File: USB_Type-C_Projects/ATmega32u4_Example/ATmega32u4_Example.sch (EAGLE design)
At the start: 8 parts, among them J2 105450-0101, U1 ATMEGA32U4-AU, U2 IP4234CZ6,125

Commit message: USB connections made.
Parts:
- added C1: 1uF, MF_Passives:CAPACITOR_NP_0603
- added C10, C11, C12, C2, C7, C8, C9: 0.1uF, MF_Passives:CAPACITOR_NP_0603
- added C5, C6: 22pF, MF_Passives:CAPACITOR_NP_0603
- added R1: 5.1K, MF_Passives:RESISTOR_0603
- added R3: 22, MF_Passives:RESISTOR_0603
- added R4: 10K, MF_Passives:RESISTOR_0603
- added SW1: MF-SW-TACT-4.2MM, MF_Switches:TACT_4.2MM
- added X1: ABM3B-16.000MHZ-D-1-X-T, MF_Frequency_Control:CYRSTAL_GND_ABM3B
- C3: value 0.1uF -> 1uF; MPN MF-CAP-0603-0.1uF -> MF-CAP-0603-1uF
- C4: value 1uF -> 0.1uF; MPN MF-CAP-0603-1uF -> MF-CAP-0603-0.1uF
- R2: value 5.1K -> 22; MPN ERJ-3EKF5101V -> MF-RES-0603-22
- U1: value ATMEGA32U4-AU -> IP4234CZ6,125; device MF_IC_Digital:ATMEGA32U4-AU -> PP_Passives:IP4234CZ6; MPN (none) -> IP4234CZ6,125
- U2: value IP4234CZ6,125 -> ATMEGA32U4-AU; device PP_Passives:IP4234CZ6 -> MF_IC_Digital:ATMEGA32U4-AU; MPN IP4234CZ6,125 -> (none)
- renumbered L3 to L1, L4 to L2
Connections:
- new net N$1: R2.P$2, U2.D-
- new net N$2: R3.P$2, U2.D+
- new net N$3: C3.P$2, U2.UCAP
- new net N$4: C4.P$2, U2.AREF
- new net RESET: R4.P$2, SW1.P$1, SW1.P$2, U2.!RESET
- new net XTAL1: C5.P$1, U2.XTAL1, X1.X0
- new net XTAL2: C6.P$1, U2.XTAL2, X1.X1
- net CC1/1: now also R1.P$1; no longer R2.P$1
- net D+: now also U1.I/O1A; no longer U2.I/O1A
- net D-: now also U1.I/O1B; no longer U2.I/O1B
- net DM: now also R2.P$1, U1.I/O2B; no longer U2.I/O2B
- net DP: now also R3.P$1, U1.I/O2A; no longer U2.I/O2A
- net GND: now also C1.P$2, C10.P$2, C11.P$2, C12.P$2, C2.P$2, C3.P$1, C4.P$1, C5.P$2, C6.P$2, C7.P$2, C8.P$2, C9.P$2, R1.P$2, SW1.P$3, SW1.P$4, U1.GND, U2.UGND, X1.GND; no longer C3.P$2, C4.P$2, R2.P$2
- net USB_VBUS: now also C1.P$1, C10.P$1, C11.P$1, C12.P$1, C2.P$1, C7.P$1, C8.P$1, C9.P$1, R4.P$1, U1.VB, U2.AVCC, U2.UVCC, U2.VBUS, U2.VCC; no longer C3.P$1, C4.P$1, U2.VB
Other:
- moved on the sheet: C3, C4, R2

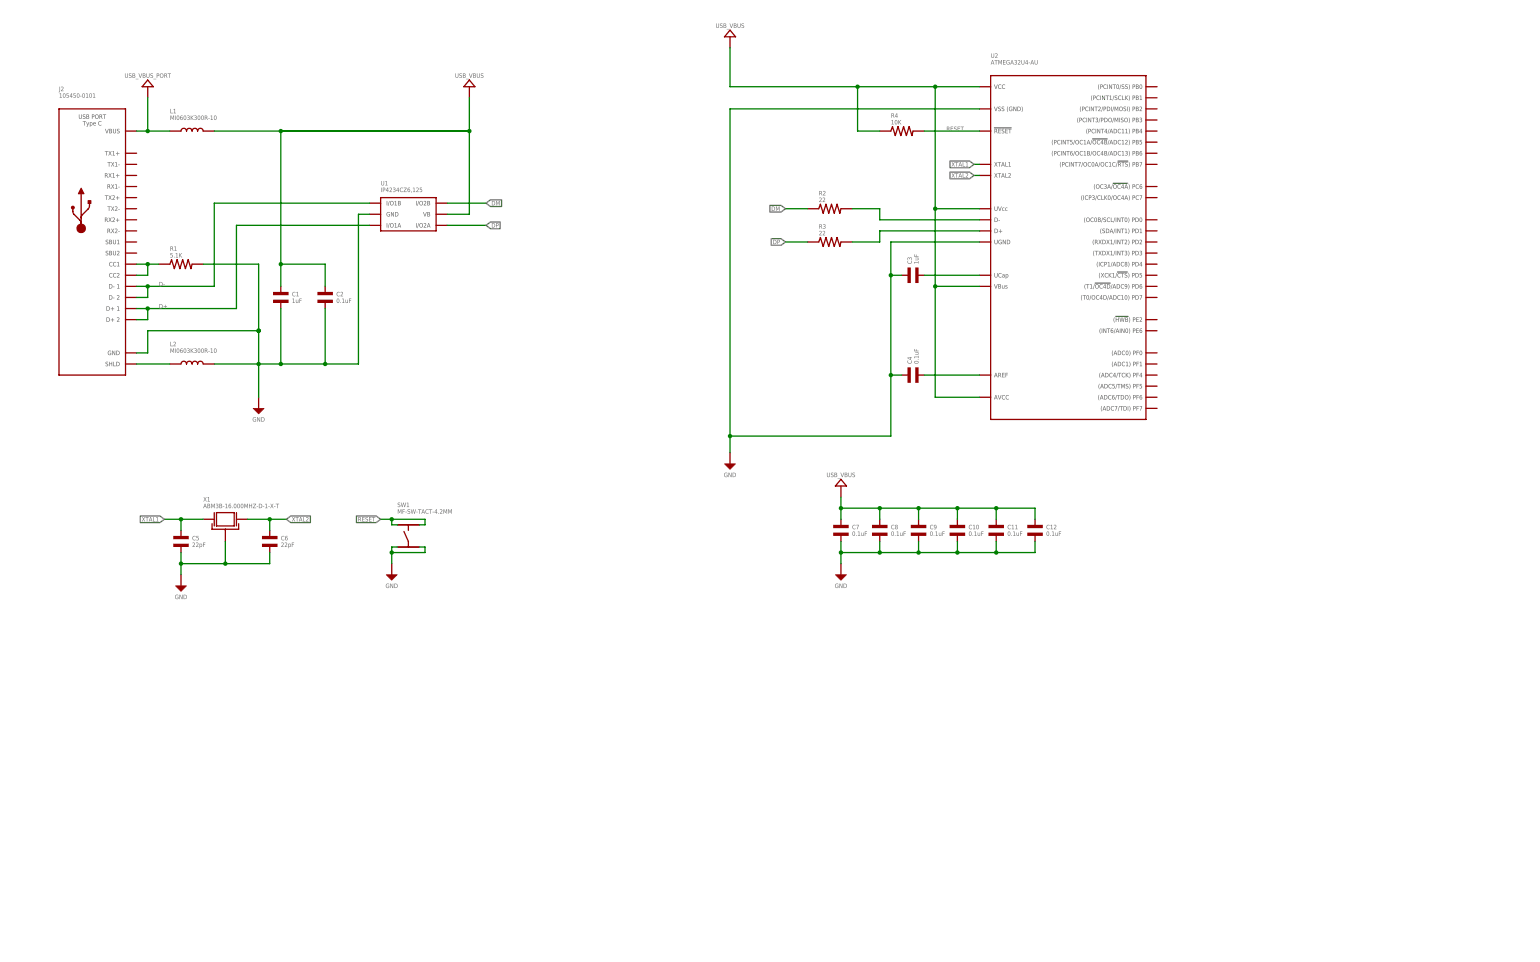
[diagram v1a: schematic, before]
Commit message: Schematic complete. Parts placed.
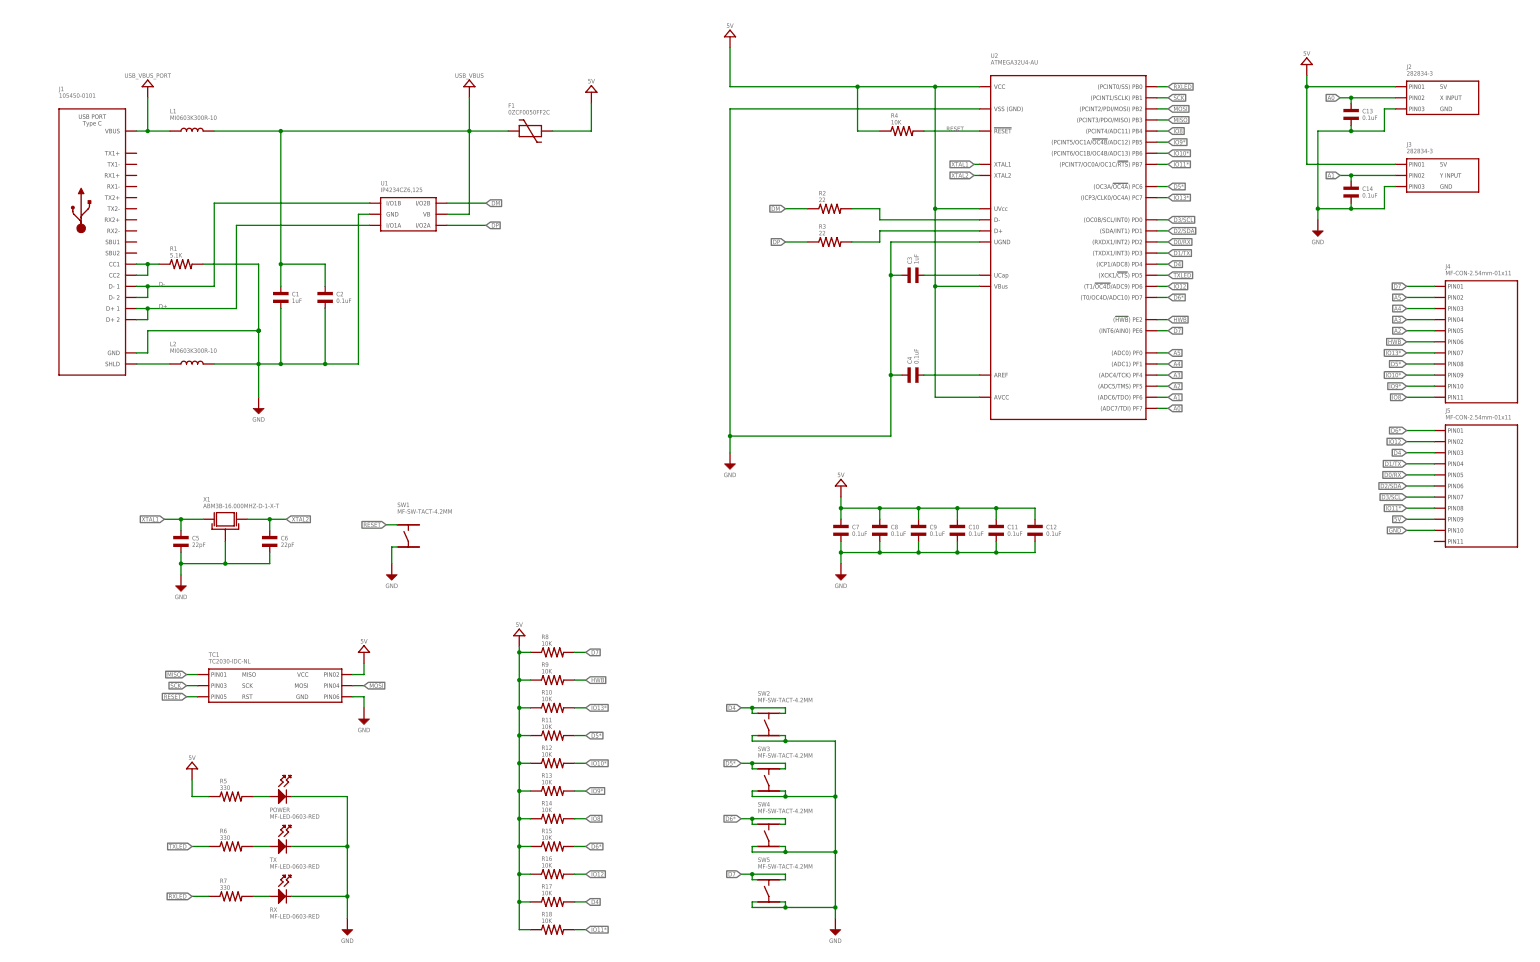
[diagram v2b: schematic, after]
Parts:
- added C13, C14: 0.1uF, MF_Passives:CAPACITOR_NP_0603
- added F1: 0ZCF0050FF2C, PP_Passives:PTC_FUSE_2920
- added J1: 105450-0101, PP_Connectors:USB_TYPE-C_105450-0101
- added J3: 282834-3, PP_Connectors:CON_01X03_282834-3
- added J4, J5: MF-CON-2.54mm-01x11, MF_Connectors:CON_01X11_PTH_2.54MM
- added POWER, RX, TX: MF-LED-0603-RED, MF_LEDs:LED_SINGLE-0603-RED
- added R10, R11, R12, R13, R14, R15, R16, R17, R18, R8, R9: 10K, MF_Passives:RESISTOR_0603
- added R5, R6, R7: 330, MF_Passives:RESISTOR_0603
- added SW2, SW3, SW4, SW5: MF-SW-TACT-4.2MM, MF_Switches:TACT_4.2MM
- added TC1: TC2030-IDC-NL, MF_Connectors:CON_02X03_AVRISP_TC2030-IDC-NL
- J2: value 105450-0101 -> 282834-3; device PP_Connectors:USB_TYPE-C_105450-0101 -> PP_Connectors:CON_01X03_282834-3; LABEL01 (none) -> 5V; LABEL02 (none) -> X INPUT; LABEL03 (none) -> GND; MPN 105450-0101 -> (none)
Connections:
- new net 5V: C10.P$1, C11.P$1, C12.P$1, C7.P$1, C8.P$1, C9.P$1, F1.P$2, J2.PIN1, J3.PIN1, J5.PIN9, R10.P$1, R11.P$1, R12.P$1, R13.P$1, R14.P$1, R15.P$1, R16.P$1, R17.P$1, R18.P$1, R4.P$1, R5.P$1, R8.P$1, R9.P$1, TC1.PIN2, U2.AVCC, U2.UVCC, U2.VBUS, U2.VCC
- new net A0: C13.P$1, J2.PIN2, U2.PF7
- new net A1: C14.P$1, J3.PIN2, U2.PF6
- new net A2: J4.PIN5, U2.PF5
- new net A3: J4.PIN4, U2.PF4
- new net A4: J4.PIN3, U2.PF1
- new net A5: J4.PIN2, U2.PF0
- new net D0/RX: J5.PIN5, U2.PD2
- new net D1/TX: J5.PIN4, U2.PD3
- new net D2/SDA: J5.PIN6, U2.PD1
- new net D3/SCL: J5.PIN7, U2.PD0
- new net D4: J5.PIN3, R17.P$2, SW2.P$1, SW2.P$2, U2.PD4
- new net D5*: J4.PIN8, R11.P$2, SW3.P$1, SW3.P$2, U2.PC6
- new net D6*: J5.PIN1, R15.P$2, SW4.P$1, SW4.P$2, U2.PD7
- new net D7: J4.PIN1, R8.P$2, SW5.P$1, SW5.P$2, U2.PE6
- new net HWB: J4.PIN6, R9.P$2, U2.PE2
- new net IO10*: J4.PIN9, R12.P$2, U2.PB6
- new net IO11*: J5.PIN8, R18.P$2, U2.PB7
- new net IO12: J5.PIN2, R16.P$2, U2.PD6
- new net IO13*: J4.PIN7, R10.P$2, U2.PC7
- new net IO8: J4.PIN11, R14.P$2, U2.PB4
- new net IO9*: J4.PIN10, R13.P$2, U2.PB5
- new net MISO: TC1.PIN1, U2.PB3
- new net MOSI: TC1.PIN4, U2.PB2
- new net N$5: POWER.ANODE, R5.P$2
- new net N$6: R6.P$2, TX.ANODE
- new net N$7: R7.P$2, RX.ANODE
- new net RXLED: R7.P$1, U2.PB0
- new net SCK: TC1.PIN3, U2.PB1
- new net TXLED: R6.P$1, U2.PD5
- net CC1/1: now also J1.CC1, J1.CC2; no longer J2.CC1, J2.CC2
- net D+: now also J1.D+1, J1.D+2; no longer J2.D+1, J2.D+2
- net D-: now also J1.D-1, J1.D-2; no longer J2.D-1, J2.D-2
- net GND: now also C13.P$2, C14.P$2, J1.GND, J2.PIN3, J3.PIN3, J5.PIN10, POWER.CATHODE, RX.CATHODE, SW2.P$3, SW2.P$4, SW3.P$3, SW3.P$4, SW4.P$3, SW4.P$4, SW5.P$3, SW5.P$4, TC1.PIN6, TX.CATHODE; no longer J2.GND, SW1.P$4
- net RESET: now also TC1.PIN5; no longer SW1.P$2
- net SHEILD1: now also J1.SHLD; no longer J2.SHLD
- net USB_VBUS: now also F1.P$1; no longer C10.P$1, C11.P$1, C12.P$1, C7.P$1, C8.P$1, C9.P$1, R4.P$1, U2.AVCC, U2.UVCC, U2.VBUS, U2.VCC
- net USB_VBUS_PORT: now also J1.VBUS; no longer J2.VBUS

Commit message: Routing complete
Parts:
- removed SW2, SW3, SW4, SW5: MF-SW-TACT-4.2MM, MF_Switches:TACT_4.2MM
- added C15: 0.1uF, MF_Passives:CAPACITOR_NP_0603
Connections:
- net 5V: now also R6.P$1, R7.P$1
- net D4: no longer SW2.P$1, SW2.P$2
- net D5*: no longer SW3.P$1, SW3.P$2
- net D6*: no longer SW4.P$1, SW4.P$2
- net D7: no longer SW5.P$1, SW5.P$2
- net GND: now also C15.P$2, J5.PIN11; no longer RX.CATHODE, SW2.P$3, SW2.P$4, SW3.P$3, SW3.P$4, SW4.P$3, SW4.P$4, SW5.P$3, SW5.P$4, TX.CATHODE
- net RESET: now also C15.P$1
- net RXLED: now also RX.CATHODE; no longer R7.P$1
- net TXLED: now also TX.CATHODE; no longer R6.P$1
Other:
- moved on the sheet: R4

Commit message: PCB complete. First rev ordered.
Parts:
- added FRAME1: MF_FRAMEDEFAULT, MF_Aesthetics:MF_FRAMEDEFAULT
- added H1, H2, H3, H4: MOUNT_HOLE150MIL, PP_Connectors:MOUNT_HOLE150MIL
- J4: LABEL01 (none) -> D7; LABEL02 (none) -> A5; LABEL03 (none) -> A4; LABEL04 (none) -> A3; LABEL05 (none) -> A2; LABEL06 (none) -> HWB; LABEL07 (none) -> IO13; LABEL08 (none) -> D5; LABEL09 (none) -> IO10; LABEL10 (none) -> IO9; LABEL11 (none) -> IO8
- J5: LABEL01 (none) -> D6; LABEL02 (none) -> IO12; LABEL03 (none) -> D4; LABEL04 (none) -> D1/TX; LABEL05 (none) -> D0/RX; LABEL06 (none) -> D2/SDA; LABEL07 (none) -> D3/SCL; LABEL08 (none) -> IO11; LABEL09 (none) -> 5V; LABEL10 (none) -> GND; LABEL11 (none) -> GND
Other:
- note added: "ATMEGA32U4 MCU"
- note added: "BREAKOUT I/O"
- note added: "BYPASS CAPS FOR MCU"
- note added: "CRYSTAL AND LOADING CAPS"
- note added: "ISP TAG-CONNECT"
- note added: "LEDS"
- note added: "MOUNTING HOLES"
- note added: "POTENTIOMETER INPUTS"
- note added: "PULL UP RESISTORS FOR I/O"
- note added: "RESET SWITCH"
- note added: "USB TYPE-C CONNECTOR"
- moved on the sheet: C10, C11, C12, C13, C14, C5, C6, C7, C8, C9, J2, J3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

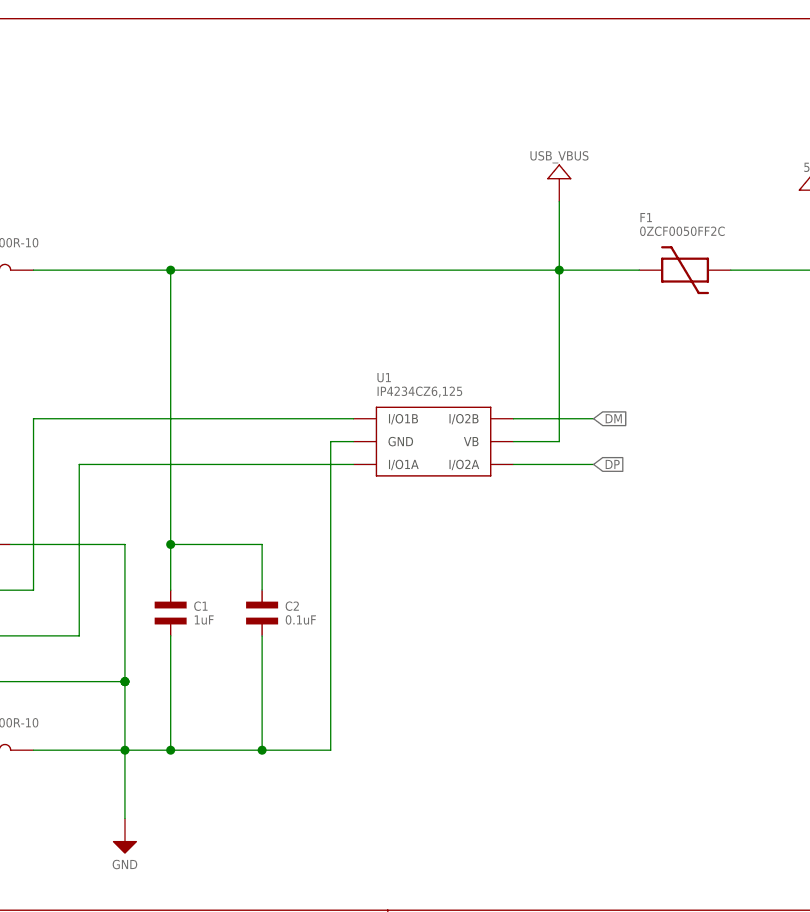
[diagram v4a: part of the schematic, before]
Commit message: Fixed IP4234CZ6 ESD protection
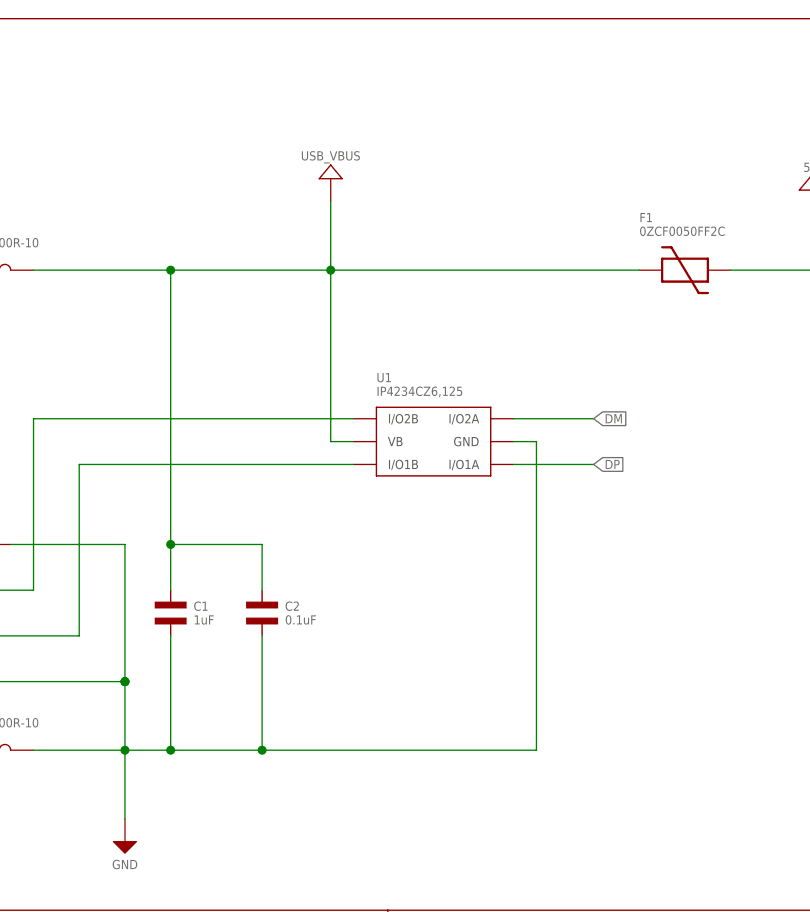
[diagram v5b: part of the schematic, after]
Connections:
- net D+: now also U1.I/O1B; no longer U1.I/O1A
- net D-: now also U1.I/O2B; no longer U1.I/O1B
- net DM: now also U1.I/O2A; no longer U1.I/O2B
- net DP: now also U1.I/O1A; no longer U1.I/O2A
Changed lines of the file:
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@@
 <attribute name="VALUE" x="19.05" y="190.5" size="1.016" layer="96" font="vector" align="center"/>
 </instance>
-<instance part="U$6" gate="G$1" x="92.71" y="187.96" smashed="yes">
-<attribute name="VALUE" x="92.71" y="190.5" size="1.016" layer="96" font="vector" align="center"/>
+<instance part="U$6" gate="G$1" x="67.31" y="187.96" smashed="yes">
+<attribute name="VALUE" x="67.31" y="190.5" size="1.016" layer="96" font="vector" align="center"/>
 </instance>
 <instance part="R1" gate="G$1" x="26.67" y="147.32" smashed="yes" rot="R90">
@@
 <attribute name="VALUE" x="24.13" y="127" size="1.016" layer="96" font="vector"/>
 </instance>
-<instance part="U1" gate="G$1" x="72.39" y="156.21" smashed="yes" rot="MR180">
+<instance part="U1" gate="G$1" x="85.09" y="156.21" smashed="yes" rot="R180">
 <attribute name="NAME" x="72.39" y="166.37" size="1.016" layer="95" font="vector" align="top-left"/>
 <attribute name="VALUE" x="72.39" y="163.83" size="1.016" layer="96" font="vector"/>
-<attribute name="MPN" x="72.39" y="156.21" size="1.016" layer="96" rot="MR180" display="off"/>
+<attribute name="MPN" x="85.09" y="156.21" size="1.016" layer="96" rot="R180" display="off"/>
 </instance>
 <instance part="U2" gate="G$1" x="212.09" y="190.5" smashed="yes">
@@
 <wire x1="44.45" y1="116.84" x2="44.45" y2="124.46" width="0.1524" layer="91"/>
 <wire x1="49.53" y1="124.46" x2="59.69" y2="124.46" width="0.1524" layer="91"/>
-<wire x1="59.69" y1="124.46" x2="67.31" y2="124.46" width="0.1524" layer="91"/>
+<wire x1="59.69" y1="124.46" x2="90.17" y2="124.46" width="0.1524" layer="91"/>
 <pinref part="C1" gate="G$1" pin="P$2"/>
 <wire x1="49.53" y1="137.16" x2="49.53" y2="124.46" width="0.1524" layer="91"/>
@@
 <pinref part="R1" gate="G$1" pin="P$2"/>
 <pinref part="L2" gate="G$1" pin="P$2"/>
+<wire x1="90.17" y1="158.75" x2="90.17" y2="124.46" width="0.1524" layer="91"/>
 <pinref part="U1" gate="G$1" pin="GND"/>
-<wire x1="69.85" y1="158.75" x2="67.31" y2="158.75" width="0.1524" layer="91"/>
-<wire x1="67.31" y1="158.75" x2="67.31" y2="124.46" width="0.1524" layer="91"/>
+<wire x1="87.63" y1="158.75" x2="90.17" y2="158.75" width="0.1524" layer="91"/>
 </segment>
 <segment>
@@
 <wire x1="19.05" y1="134.62" x2="16.51" y2="134.62" width="0.1524" layer="91"/>
 <junction x="19.05" y="137.16"/>
-<pinref part="U1" gate="G$1" pin="I/O1A"/>
 <wire x1="39.37" y1="156.21" x2="69.85" y2="156.21" width="0.1524" layer="91"/>
+<pinref part="U1" gate="G$1" pin="I/O1B"/>
 </segment>
 </net>
@@
 <wire x1="19.05" y1="139.7" x2="16.51" y2="139.7" width="0.1524" layer="91"/>
 <junction x="19.05" y="142.24"/>
-<pinref part="U1" gate="G$1" pin="I/O1B"/>
 <wire x1="34.29" y1="161.29" x2="69.85" y2="161.29" width="0.1524" layer="91"/>
+<pinref part="U1" gate="G$1" pin="I/O2B"/>
 </segment>
 </net>
@@
 <wire x1="59.69" y1="147.32" x2="49.53" y2="147.32" width="0.1524" layer="91"/>
 <wire x1="49.53" y1="147.32" x2="49.53" y2="177.8" width="0.1524" layer="91"/>
-<wire x1="49.53" y1="177.8" x2="92.71" y2="177.8" width="0.1524" layer="91"/>
+<wire x1="49.53" y1="177.8" x2="67.31" y2="177.8" width="0.1524" layer="91"/>
 <pinref part="C1" gate="G$1" pin="P$1"/>
 <wire x1="49.53" y1="147.32" x2="49.53" y2="142.24" width="0.1524" layer="91"/>
 <junction x="49.53" y="147.32"/>
-<junction x="92.71" y="177.8"/>
+<junction x="67.31" y="177.8"/>
 <pinref part="U$6" gate="G$1" pin="P$1"/>
-<wire x1="92.71" y1="185.42" x2="92.71" y2="177.8" width="0.1524" layer="91"/>
+<wire x1="67.31" y1="185.42" x2="67.31" y2="177.8" width="0.1524" layer="91"/>
 <pinref part="L1" gate="G$1" pin="P$2"/>
-<pinref part="U1" gate="G$1" pin="VB"/>
-<wire x1="87.63" y1="158.75" x2="92.71" y2="158.75" width="0.1524" layer="91"/>
-<wire x1="92.71" y1="158.75" x2="92.71" y2="177.8" width="0.1524" layer="91"/>
+<wire x1="67.31" y1="158.75" x2="67.31" y2="177.8" width="0.1524" layer="91"/>
 <junction x="49.53" y="177.8"/>
 <pinref part="F1" gate="G$1" pin="P$1"/>
-<wire x1="92.71" y1="177.8" x2="101.6" y2="177.8" width="0.1524" layer="91"/>
+<wire x1="67.31" y1="177.8" x2="101.6" y2="177.8" width="0.1524" layer="91"/>
+<pinref part="U1" gate="G$1" pin="VB"/>
+<wire x1="67.31" y1="158.75" x2="69.85" y2="158.75" width="0.1524" layer="91"/>
 </segment>
 </net>
 <net name="DP" class="0">
 <segment>
-<pinref part="U1" gate="G$1" pin="I/O2A"/>
 <wire x1="87.63" y1="156.21" x2="96.52" y2="156.21" width="0.1524" layer="91"/>
 <label x="96.52" y="156.21" size="1.016" layer="95" font="vector" xref="yes"/>
+<pinref part="U1" gate="G$1" pin="I/O1A"/>
 </segment>
 <segment>
@@
 <net name="DM" class="0">
 <segment>
-<pinref part="U1" gate="G$1" pin="I/O2B"/>
 <wire x1="87.63" y1="161.29" x2="96.52" y2="161.29" width="0.1524" layer="91"/>
 <label x="96.52" y="161.29" size="1.016" layer="95" font="vector" xref="yes"/>
-</segment>
-<segment>
+<pinref part="U1" gate="G$1" pin="I/O2A"/>
+</segment>
+<segment>

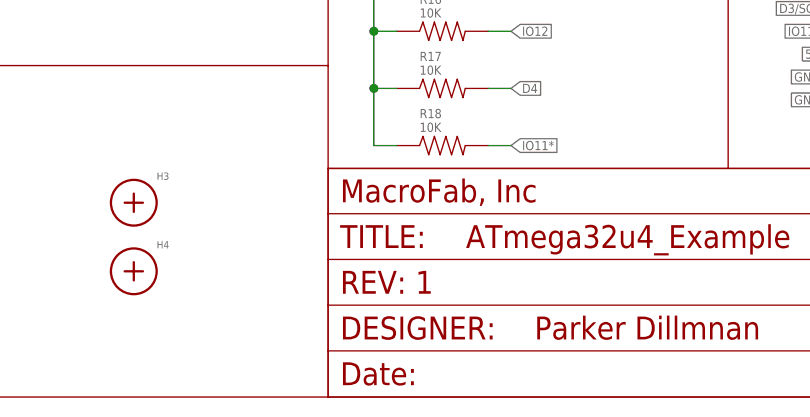
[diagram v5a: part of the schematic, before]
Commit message: REV 2. Fixed USB ESD protection.
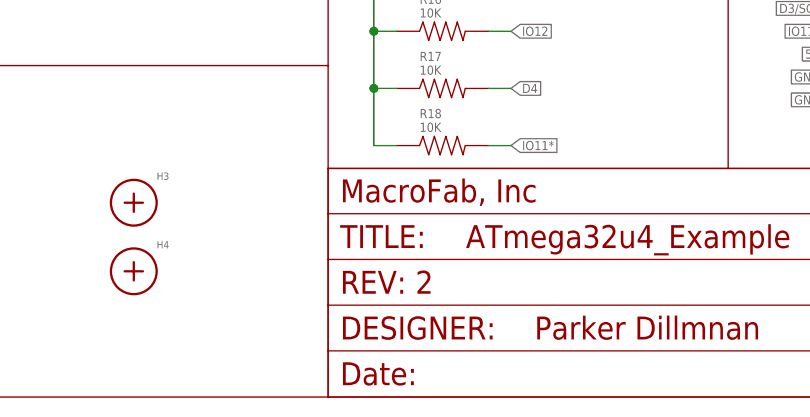
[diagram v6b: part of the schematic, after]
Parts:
- FRAME1: REVNUM REV: 1 -> REV: 2
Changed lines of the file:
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@@
 <?xml version="1.0" encoding="utf-8"?>
 <!DOCTYPE eagle SYSTEM "eagle.dtd">
-<eagle version="9.3.0">
+<eagle version="9.3.2">
 <drawing>
 <settings>
@@
 <part name="FRAME1" library="MF_Aesthetics" deviceset="MF_FRAME" device="DEFAULT">
 <attribute name="DNAME" value="Parker Dillmnan"/>
-<attribute name="REVNUM" value="REV: 1"/>
+<attribute name="REVNUM" value="REV: 2"/>
 </part>
 </parts>
